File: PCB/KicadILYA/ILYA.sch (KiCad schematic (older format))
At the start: 4 parts, among them U1 NodeMCU1.0(ESP-12E), U2 Relay_2_pins, U3101 Flow_connector

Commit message: Routage Bon mais connexion pins?
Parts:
- U1: symbol ESP8266:NodeMCU1.0(ESP-12E) -> ILYA-rescue:NodeMCU1.0(ESP-12E)-ESP8266
- U101: renamed from U?; footprint (none) -> pinHeads:PinHeader_1x04_P2.54mm_Horizontal; symbol MyConnectors:Temperature_connector -> ILYA-rescue:Temperature_connector-MyConnectors
- U2: footprint (none) -> pinHeads:PinHeader_1x02_P2.54mm_Horizontal; symbol MyRelay:Relay_2_pins -> ILYA-rescue:Relay_2_pins-MyRelay
- U3101: footprint (none) -> pinHeads:PinHeader_1x03_P2.54mm_Horizontal; symbol MyConnectors:Flow_connector -> ILYA-rescue:Flow_connector-MyConnectors
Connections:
- net labels added: +5V, GND, VCC
- wire segments 22 -> 8
- no-connect marks 23 -> 26
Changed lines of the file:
@@
 EESchema Schematic File Version 4
+LIBS:ILYA-cache
 EELAYER 26 0
 EELAYER END
@@
 $EndDescr
 $Comp
-L ESP8266:NodeMCU1.0(ESP-12E) U1
-U 1 1 5DF783D9
-P 4550 2700
-F 0 "U1" V 4603 1772 60  0000 R CNN
-F 1 "NodeMCU1.0(ESP-12E)" V 4497 1772 60  0000 R CNN
-F 2 "nodemcu:SEEED_113990105" H 3950 1850 60  0001 C CNN
-F 3 "" H 3950 1850 60  0000 C CNN
-	1    4550 2700
-	0    -1   -1   0
-$EndComp
-$Comp
-L MyRelay:Relay_2_pins U2
+L ILYA-rescue:Relay_2_pins-MyRelay U2
 U 1 1 5DF78856
-P 5350 4150
-F 0 "U2" H 5312 3843 50  0000 R CNN
-F 1 "Relay_2_pins" H 5312 3934 50  0000 R CNN
-F 2 "" H 5350 4150 50  0001 C CNN
-F 3 "" H 5350 4150 50  0001 C CNN
-	1    5350 4150
-	-1   0    0    1
-$EndComp
-$Comp
-L MyConnectors:Flow_connector U3101
+P 5600 4600
+F 0 "U2" H 5562 4293 50  0000 R CNN
+F 1 "Relay_2_pins" H 5562 4384 50  0000 R CNN
+F 2 "pinHeads:PinHeader_1x02_P2.54mm_Horizontal" H 5600 4600 50  0001 C CNN
+F 3 "" H 5600 4600 50  0001 C CNN
+	1    5600 4600
+	-1   0    0    1
+$EndComp
+$Comp
+L ILYA-rescue:Flow_connector-MyConnectors U3101
 U 1 1 5DF78A93
-P 5200 1200
-F 0 "U3101" H 5278 1110 50  0000 L CNN
-F 1 "Flow_connector" H 5278 1019 50  0000 L CNN
-F 2 "" H 5200 1200 50  0001 C CNN
-F 3 "" H 5200 1200 50  0001 C CNN
-	1    5200 1200
+P 4850 1000
+F 0 "U3101" H 4928 785 50  0000 L CNN
+F 1 "Flow_connector" H 4928 694 50  0000 L CNN
+F 2 "pinHeads:PinHeader_1x03_P2.54mm_Horizontal" H 4850 1000 50  0001 C CNN
+F 3 "" H 4850 1000 50  0001 C CNN
+	1    4850 1000
 	1    0    0    -1
 $EndComp
@@
 Wire Wire Line
 	3850 3650 3800 3650
-Wire Wire Line
-	5200 1550 5200 1700
-Wire Wire Line
-	5200 1700 5250 1700
-Wire Wire Line
-	5250 1700 5250 1900
-Wire Wire Line
-	5100 1550 5100 1750
-Wire Wire Line
-	5100 1750 5150 1750
-Wire Wire Line
-	5150 1750 5150 1900
-Wire Wire Line
-	4550 1900 4550 1700
-Wire Wire Line
-	4550 1700 5050 1700
-Wire Wire Line
-	5050 1700 5050 1550
-Wire Wire Line
-	5150 3500 5150 3700
-Wire Wire Line
-	5250 3500 5250 3650
-Wire Wire Line
-	5250 3650 5300 3650
-Wire Wire Line
-	5300 3650 5300 3700
-Wire Wire Line
-	3800 3650 3800 3750
-Wire Wire Line
-	4850 3650 4850 3500
-Wire Wire Line
-	4750 3500 4750 3600
-$Comp
-L MyConnectors:Temperature_connector U?
+$Comp
+L ILYA-rescue:Temperature_connector-MyConnectors U101
 U 1 1 5DF80F41
-P 3800 4150
-F 0 "U?" H 3412 3872 50  0000 R CNN
-F 1 "Temperature_connector" H 3412 3963 50  0000 R CNN
-F 2 "" H 3800 4150 50  0001 C CNN
-F 3 "" H 3800 4150 50  0001 C CNN
-	1    3800 4150
-	-1   0    0    1
-$EndComp
-Wire Wire Line
-	4850 3650 4100 3650
-Wire Wire Line
-	4100 3650 4100 3750
-Wire Wire Line
-	4750 3600 4000 3600
-Wire Wire Line
-	4000 3600 4000 3750
-NoConn ~ 3900 3750
+P 3800 4300
+F 0 "U101" H 3412 4022 50  0000 R CNN
+F 1 "Temperature_connector" H 3412 4113 50  0000 R CNN
+F 2 "pinHeads:PinHeader_1x04_P2.54mm_Horizontal" H 3800 4300 50  0001 C CNN
+F 3 "" H 3800 4300 50  0001 C CNN
+	1    3800 4300
+	-1   0    0    1
+$EndComp
 NoConn ~ 3850 1900
 NoConn ~ 3950 1900
@@
 NoConn ~ 4150 1900
 NoConn ~ 4250 1900
-NoConn ~ 4350 1900
-NoConn ~ 4450 1900
 NoConn ~ 4650 1900
 NoConn ~ 4750 1900
@@
 NoConn ~ 4950 1900
 NoConn ~ 5050 1900
-NoConn ~ 3950 3500
 NoConn ~ 4050 3500
 NoConn ~ 4150 3500
@@
 NoConn ~ 4950 3500
 NoConn ~ 5050 3500
+$Comp
+L power:+5V #PWR0101
+U 1 1 5DFBDC88
+P 3000 1350
+F 0 "#PWR0101" H 3000 1200 50  0001 C CNN
+F 1 "+5V" H 3015 1523 50  0000 C CNN
+F 2 "" H 3000 1350 50  0001 C CNN
+F 3 "" H 3000 1350 50  0001 C CNN
+	1    3000 1350
+	-1   0    0    1
+$EndComp
+$Comp
+L power:GND #PWR0102
+U 1 1 5DFBDF30
+P 3400 1350
+F 0 "#PWR0102" H 3400 1100 50  0001 C CNN
+F 1 "GND" H 3405 1177 50  0000 C CNN
+F 2 "" H 3400 1350 50  0001 C CNN
+F 3 "" H 3400 1350 50  0001 C CNN
+	1    3400 1350
+	1    0    0    -1
+$EndComp
+$Comp
+L power:PWR_FLAG #FLG0102
+U 1 1 5DFBE02B
+P 3400 1150
+F 0 "#FLG0102" H 3400 1225 50  0001 C CNN
+F 1 "PWR_FLAG" H 3400 1324 50  0000 C CNN
+F 2 "" H 3400 1150 50  0001 C CNN
+F 3 "~" H 3400 1150 50  0001 C CNN
+	1    3400 1150
+	1    0    0    -1
+$EndComp
+$Comp
+L power:PWR_FLAG #FLG0101
+U 1 1 5DFBE05D
+P 3000 1150
+F 0 "#FLG0101" H 3000 1225 50  0001 C CNN
+F 1 "PWR_FLAG" H 3000 1324 50  0000 C CNN
+F 2 "" H 3000 1150 50  0001 C CNN
+F 3 "~" H 3000 1150 50  0001 C CNN
+	1    3000 1150
+	1    0    0    -1
+$EndComp
+Wire Wire Line
+	3000 1150 3000 1350
+Text GLabel 5250 1900 1    50   Input ~ 0
+VCC
+Wire Wire Line
+	3800 3650 3800 3900
+Wire Wire Line
+	4700 1400 4700 1650
+Wire Wire Line
+	4700 1650 4550 1650
+Wire Wire Line
+	4550 1650 4550 1900
+Text GLabel 4850 1400 3    50   Input ~ 0
+VCC
+NoConn ~ 3950 3500
+NoConn ~ 3900 3900
+$Comp
+L power:GND #PWR0103
+U 1 1 5DFC6197
+P 5400 4150
+F 0 "#PWR0103" H 5400 3900 50  0001 C CNN
+F 1 "GND" H 5405 3977 50  0000 C CNN
+F 2 "" H 5400 4150 50  0001 C CNN
+F 3 "" H 5400 4150 50  0001 C CNN
+	1    5400 4150
+	-1   0    0    1
+$EndComp
+$Comp
+L power:+5V #PWR0104
+U 1 1 5DFC6254
+P 5550 4150
+F 0 "#PWR0104" H 5550 4000 50  0001 C CNN
+F 1 "+5V" H 5565 4323 50  0000 C CNN
+F 2 "" H 5550 4150 50  0001 C CNN
+F 3 "" H 5550 4150 50  0001 C CNN
+	1    5550 4150
+	1    0    0    -1
+$EndComp
+$Comp
+L power:+5V #PWR0105
+U 1 1 5DFC6C57
+P 5250 3500
+F 0 "#PWR0105" H 5250 3350 50  0001 C CNN
+F 1 "+5V" H 5265 3673 50  0000 C CNN
+F 2 "" H 5250 3500 50  0001 C CNN
+F 3 "" H 5250 3500 50  0001 C CNN
+	1    5250 3500
+	-1   0    0    1
+$EndComp
+$Comp
+L power:GND #PWR0106
+U 1 1 5DFC6E90
+P 4750 1400
+F 0 "#PWR0106" H 4750 1150 50  0001 C CNN
+F 1 "GND" H 4750 1200 50  0000 C CNN
+F 2 "" H 4750 1400 50  0001 C CNN
+F 3 "" H 4750 1400 50  0001 C CNN
+	1    4750 1400
+	1    0    0    -1
+$EndComp
+$Comp
+L power:GND #PWR0107
+U 1 1 5DFC7291
+P 4000 3900
+F 0 "#PWR0107" H 4000 3650 50  0001 C CNN
+F 1 "GND" H 4005 3727 50  0000 C CNN
+F 2 "" H 4000 3900 50  0001 C CNN
+F 3 "" H 4000 3900 50  0001 C CNN
+	1    4000 3900
+	-1   0    0    1
+$EndComp
+Text GLabel 4100 3900 1    50   Input ~ 0
+VCC
+$Comp
+L power:GND #PWR0110
+U 1 1 5DFCC369
+P 5150 3500
+F 0 "#PWR0110" H 5150 3250 50  0001 C CNN
+F 1 "GND" H 5155 3327 50  0000 C CNN
+F 2 "" H 5150 3500 50  0001 C CNN
+F 3 "" H 5150 3500 50  0001 C CNN
+	1    5150 3500
+	1    0    0    -1
+$EndComp
+Wire Wire Line
+	3400 1350 3400 1150
+NoConn ~ 4350 1900
+NoConn ~ 4450 1900
+NoConn ~ 4750 3500
+NoConn ~ 4850 3500
+$Comp
+L ILYA-rescue:NodeMCU1.0(ESP-12E)-ESP8266 U1
+U 1 1 5DF783D9
+P 4550 2700
+F 0 "U1" V 4603 1772 60  0000 R CNN
+F 1 "NodeMCU1.0(ESP-12E)" V 4497 1772 60  0000 R CNN
+F 2 "nodemcu:SEEED_113990105" H 3950 1850 60  0001 C CNN
+F 3 "" H 3950 1850 60  0000 C CNN
+	1    4550 2700
+	0    -1   -1   0
+$EndComp
+NoConn ~ 5150 1900
 $EndSCHEMATC

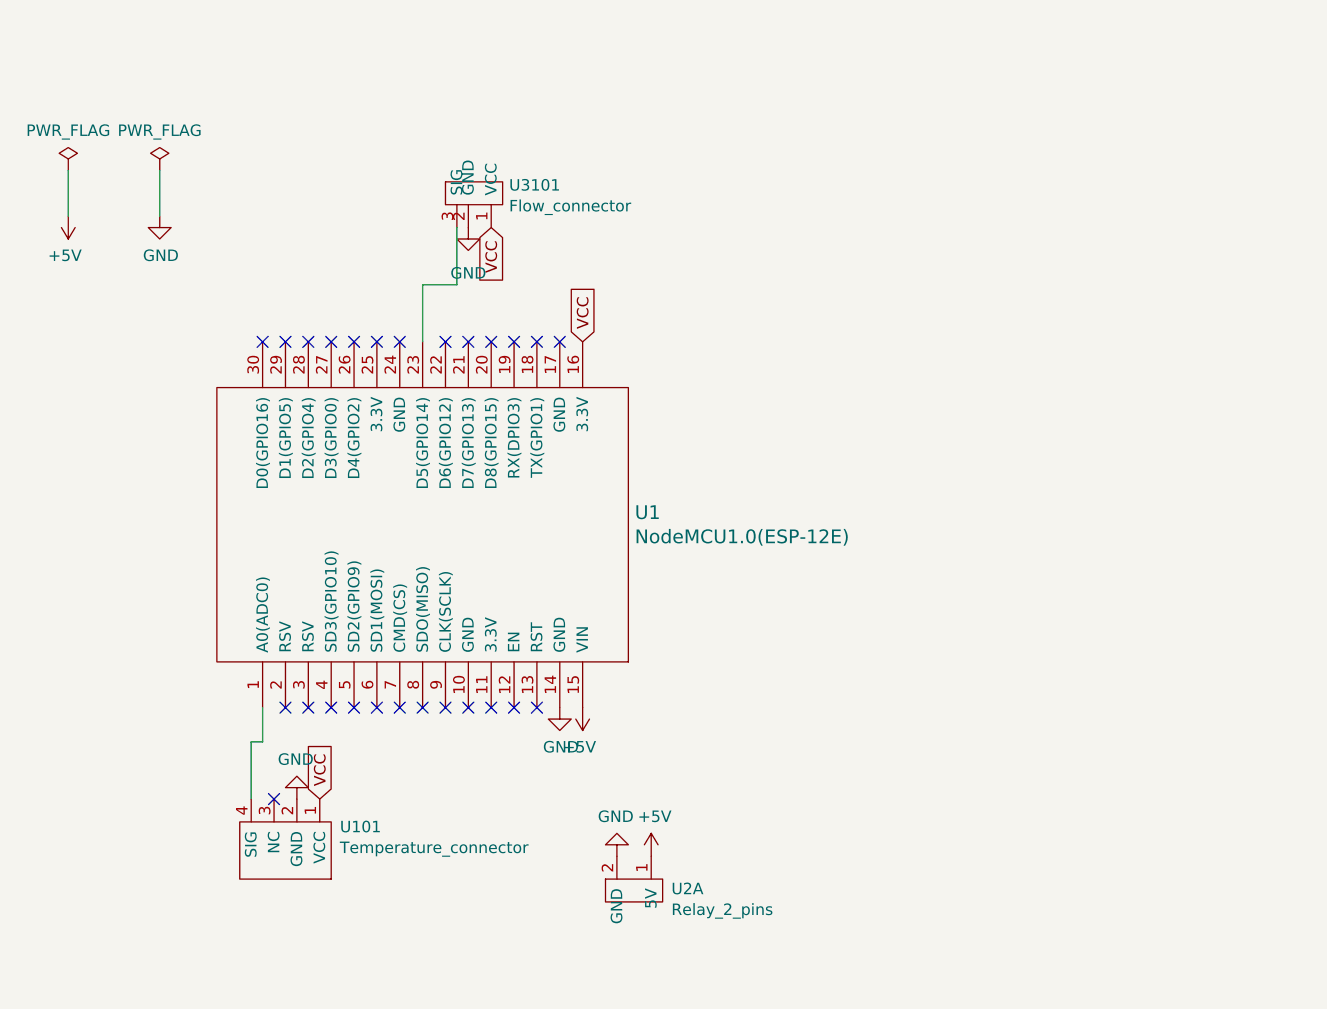
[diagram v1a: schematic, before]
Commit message: Sheild esp8266 good
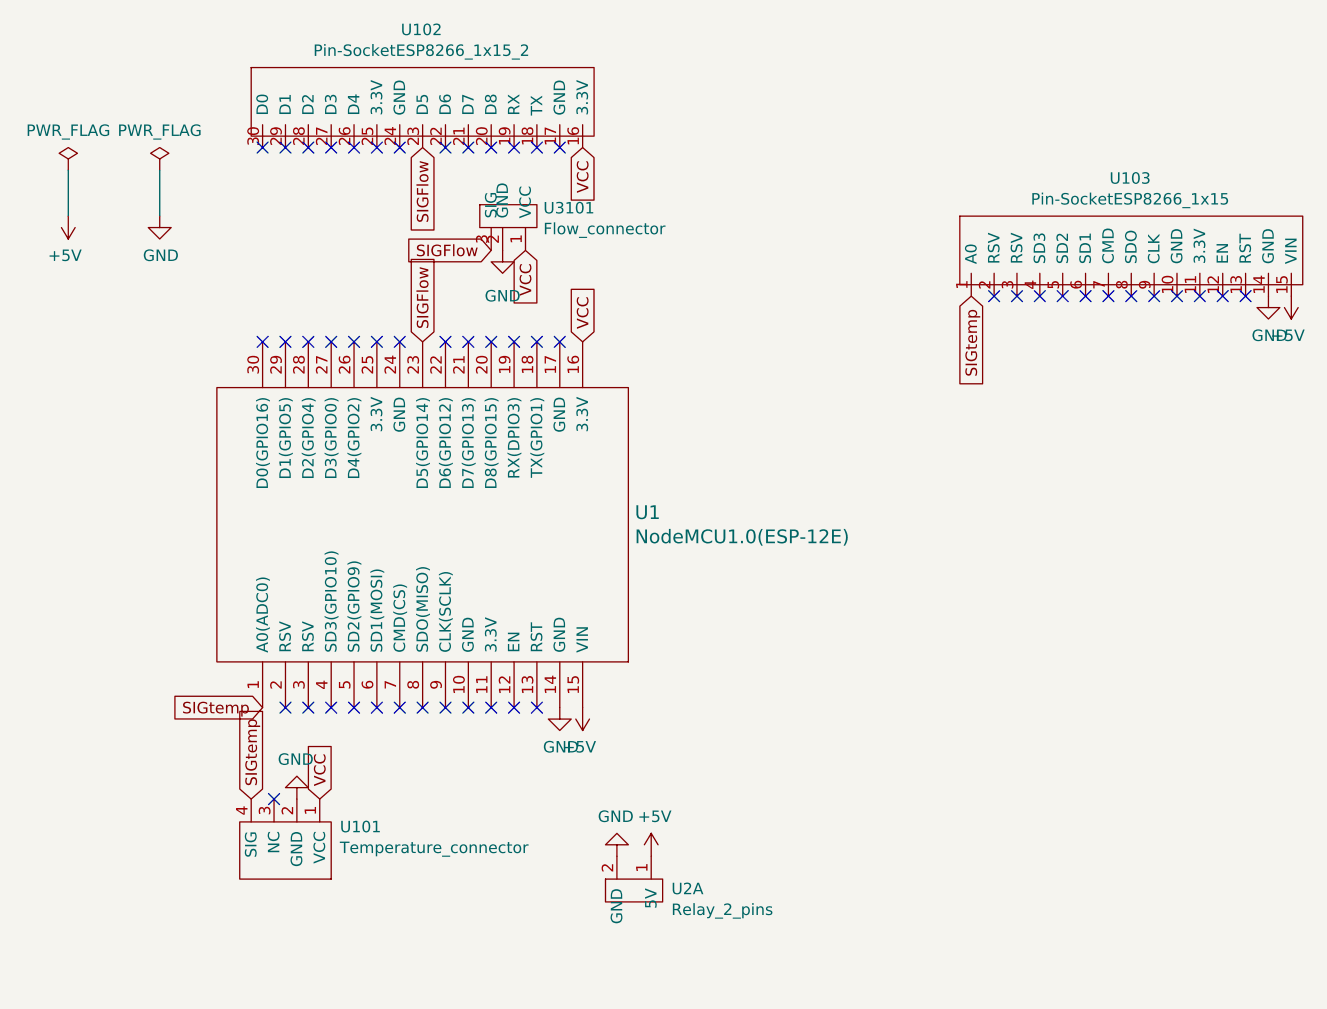
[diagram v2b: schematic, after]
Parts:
- added U102: Pin-SocketESP8266_1x15_2, pinSocket:PinSocket_1x15_P2.54mm_Vertical2, symbol MyRelay:Pin-SocketESP8266_1x15_2
- added U103: Pin-SocketESP8266_1x15, pinSocket:PinSocket_1x15_P2.54mm_Vertical, symbol MyRelay:Pin-SocketESP8266_1x15
- U1: footprint nodemcu:SEEED_113990105 -> wemos-d1-mini:SEEED_113990105_withoutPin
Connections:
- net +5V: now also U103.15 (VIN)
- net GND: now also U103.14 (GND)
- net VCC: now also U102.16 (3.3V)
- net SIGtemp: now reaches U1.1 (A0(ADC0)), U101.4 (SIG)
- net SIGtemp: now also U103.1 (A0)
- net SIGFlow: now reaches U1.23 (D5(GPIO14)), U3101.3 (SIG)
- net SIGFlow: now also U102.23 (D5)
- no-connect marks 26 -> 51
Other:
- moved on the sheet: U3101
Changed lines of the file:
@@
 L ILYA-rescue:Flow_connector-MyConnectors U3101
 U 1 1 5DF78A93
-P 4850 1000
-F 0 "U3101" H 4928 785 50  0000 L CNN
-F 1 "Flow_connector" H 4928 694 50  0000 L CNN
-F 2 "pinHeads:PinHeader_1x03_P2.54mm_Horizontal" H 4850 1000 50  0001 C CNN
-F 3 "" H 4850 1000 50  0001 C CNN
-	1    4850 1000
-	1    0    0    -1
-$EndComp
-Wire Wire Line
-	3850 3500 3850 3650
-Wire Wire Line
-	3850 3650 3800 3650
+P 5000 1100
+F 0 "U3101" H 5078 885 50  0000 L CNN
+F 1 "Flow_connector" H 5078 794 50  0000 L CNN
+F 2 "pinHeads:PinHeader_1x03_P2.54mm_Horizontal" H 5000 1100 50  0001 C CNN
+F 3 "" H 5000 1100 50  0001 C CNN
+	1    5000 1100
+	1    0    0    -1
+$EndComp
 $Comp
 L ILYA-rescue:Temperature_connector-MyConnectors U101
@@
 Text GLabel 5250 1900 1    50   Input ~ 0
 VCC
-Wire Wire Line
-	3800 3650 3800 3900
-Wire Wire Line
-	4700 1400 4700 1650
-Wire Wire Line
-	4700 1650 4550 1650
-Wire Wire Line
-	4550 1650 4550 1900
-Text GLabel 4850 1400 3    50   Input ~ 0
+Text GLabel 5000 1500 3    50   Input ~ 0
 VCC
 NoConn ~ 3950 3500
@@
 L power:GND #PWR0106
 U 1 1 5DFC6E90
-P 4750 1400
-F 0 "#PWR0106" H 4750 1150 50  0001 C CNN
-F 1 "GND" H 4750 1200 50  0000 C CNN
-F 2 "" H 4750 1400 50  0001 C CNN
-F 3 "" H 4750 1400 50  0001 C CNN
-	1    4750 1400
+P 4900 1500
+F 0 "#PWR0106" H 4900 1250 50  0001 C CNN
+F 1 "GND" H 4900 1300 50  0000 C CNN
+F 2 "" H 4900 1500 50  0001 C CNN
+F 3 "" H 4900 1500 50  0001 C CNN
+	1    4900 1500
 	1    0    0    -1
 $EndComp
@@
 F 0 "U1" V 4603 1772 60  0000 R CNN
 F 1 "NodeMCU1.0(ESP-12E)" V 4497 1772 60  0000 R CNN
-F 2 "nodemcu:SEEED_113990105" H 3950 1850 60  0001 C CNN
+F 2 "wemos-d1-mini:SEEED_113990105_withoutPin" H 3950 1850 60  0001 C CNN
 F 3 "" H 3950 1850 60  0000 C CNN
 	1    4550 2700
@@
 $EndComp
 NoConn ~ 5150 1900
+NoConn ~ 3850 1050
+NoConn ~ 3950 1050
+NoConn ~ 4050 1050
+NoConn ~ 4150 1050
+NoConn ~ 4250 1050
+NoConn ~ 4350 1050
+NoConn ~ 4450 1050
+NoConn ~ 4650 1050
+NoConn ~ 4750 1050
+NoConn ~ 4850 1050
+NoConn ~ 4950 1050
+NoConn ~ 5050 1050
+NoConn ~ 5150 1050
+NoConn ~ 7050 1700
+NoConn ~ 7150 1700
+NoConn ~ 7250 1700
+NoConn ~ 7350 1700
+NoConn ~ 7450 1700
+NoConn ~ 7550 1700
+NoConn ~ 7650 1700
+NoConn ~ 7750 1700
+NoConn ~ 7850 1700
+NoConn ~ 7950 1700
+NoConn ~ 8050 1700
+NoConn ~ 8150 1700
+Text GLabel 5250 1050 3    50   Input ~ 0
+VCC
+$Comp
+L power:GND #PWR0108
+U 1 1 5DFD19B9
+P 8250 1700
+F 0 "#PWR0108" H 8250 1450 50  0001 C CNN
+F 1 "GND" H 8255 1527 50  0000 C CNN
+F 2 "" H 8250 1700 50  0001 C CNN
+F 3 "" H 8250 1700 50  0001 C CNN
+	1    8250 1700
+	1    0    0    -1
+$EndComp
+$Comp
+L power:+5V #PWR0109
+U 1 1 5DFD19F8
+P 8350 1700
+F 0 "#PWR0109" H 8350 1550 50  0001 C CNN
+F 1 "+5V" H 8365 1873 50  0000 C CNN
+F 2 "" H 8350 1700 50  0001 C CNN
+F 3 "" H 8350 1700 50  0001 C CNN
+	1    8350 1700
+	-1   0    0    1
+$EndComp
+Text GLabel 3800 3900 1    50   Input ~ 0
+SIGtemp
+Text GLabel 3850 3500 0    50   Input ~ 0
+SIGtemp
+Text GLabel 6950 1700 3    50   Input ~ 0
+SIGtemp
+Text GLabel 4550 1050 3    50   Input ~ 0
+SIGFlow
+Text GLabel 4850 1500 0    50   Input ~ 0
+SIGFlow
+Text GLabel 4550 1900 1    50   Input ~ 0
+SIGFlow
+$Comp
+L MyRelay:Pin-SocketESP8266_1x15_2 U102
+U 1 1 5DFD48AF
+P 4800 1150
+F 0 "U102" H 4545 1765 50  0000 C CNN
+F 1 "Pin-SocketESP8266_1x15_2" H 4545 1674 50  0000 C CNN
+F 2 "pinSocket:PinSocket_1x15_P2.54mm_Vertical2" H 4800 1150 50  0001 C CNN
+F 3 "" H 4800 1150 50  0001 C CNN
+	1    4800 1150
+	1    0    0    -1
+$EndComp
+$Comp
+L MyRelay:Pin-SocketESP8266_1x15 U103
+U 1 1 5DFD4985
+P 8000 1100
+F 0 "U103" H 7645 1015 50  0000 C CNN
+F 1 "Pin-SocketESP8266_1x15" H 7645 924 50  0000 C CNN
+F 2 "pinSocket:PinSocket_1x15_P2.54mm_Vertical" H 8000 1100 50  0001 C CNN
+F 3 "" H 8000 1100 50  0001 C CNN
+	1    8000 1100
+	1    0    0    -1
+$EndComp
 $EndSCHEMATC
